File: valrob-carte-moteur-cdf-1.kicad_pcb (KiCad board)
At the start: 2 copper layers, 74 parts, among them J1 USB_C_Receptacle_USB2.0_14P, J2 Conn_01x02, J3 Conn_01x02, J4 Conn_01x04_Pin, J5 Conn_01x08, J6 Conn_01x02, J7 Conn_01x02, J8 Conn_01x08, SW1 SW_Push, SW2 SW_Push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

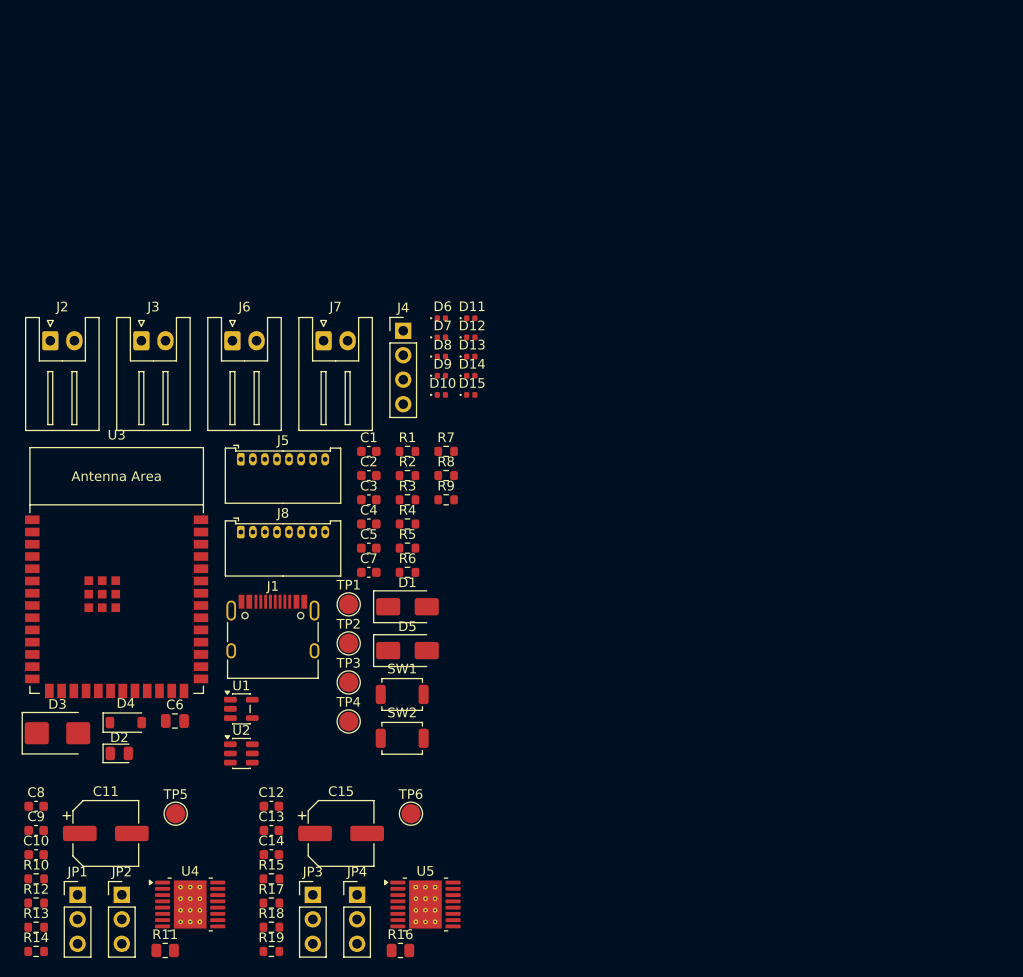
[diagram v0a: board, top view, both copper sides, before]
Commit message: pcb: initial rough placement
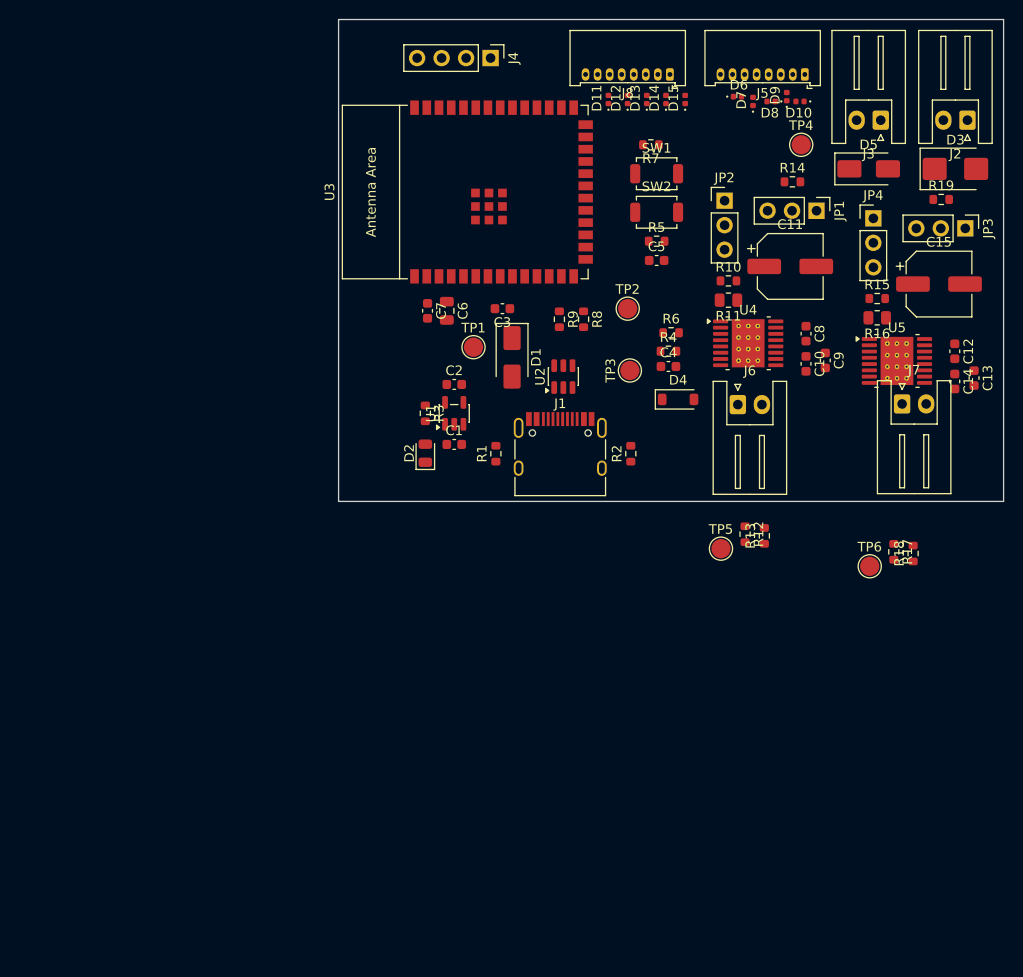
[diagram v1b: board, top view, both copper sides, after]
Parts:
- moved R14 112.0 mm to (124.1, 101.8)
- moved D3 110.0 mm to (141.0, 100.5)
- moved R19 104.5 mm to (139.5, 103.7)
- moved JP1 104.5 mm to (126.6, 104.8), turned to -90 degrees
- moved J2 97.9 mm to (142.2, 95.4), turned to 180 degrees
- moved JP3 96.8 mm to (142.0, 106.7), turned to -90 degrees
- moved JP2 95.4 mm to (117.0, 103.8)
- moved C9 95.3 mm to (127.5, 120.4), turned to -90 degrees
- moved R10 94.9 mm to (117.5, 112.1)
- moved C10 94.7 mm to (125.5, 120.7), turned to -90 degrees
- moved C8 93.7 mm to (125.5, 117.6), turned to -90 degrees
- moved C11 92.2 mm to (123.9, 110.6)
- moved R11 89.3 mm to (117.5, 114.1), turned to 180 degrees
- moved JP4 88.3 mm to (132.5, 105.6)
- moved R15 87.0 mm to (132.9, 113.9)
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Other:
- board outline added: 69 x 50 mm

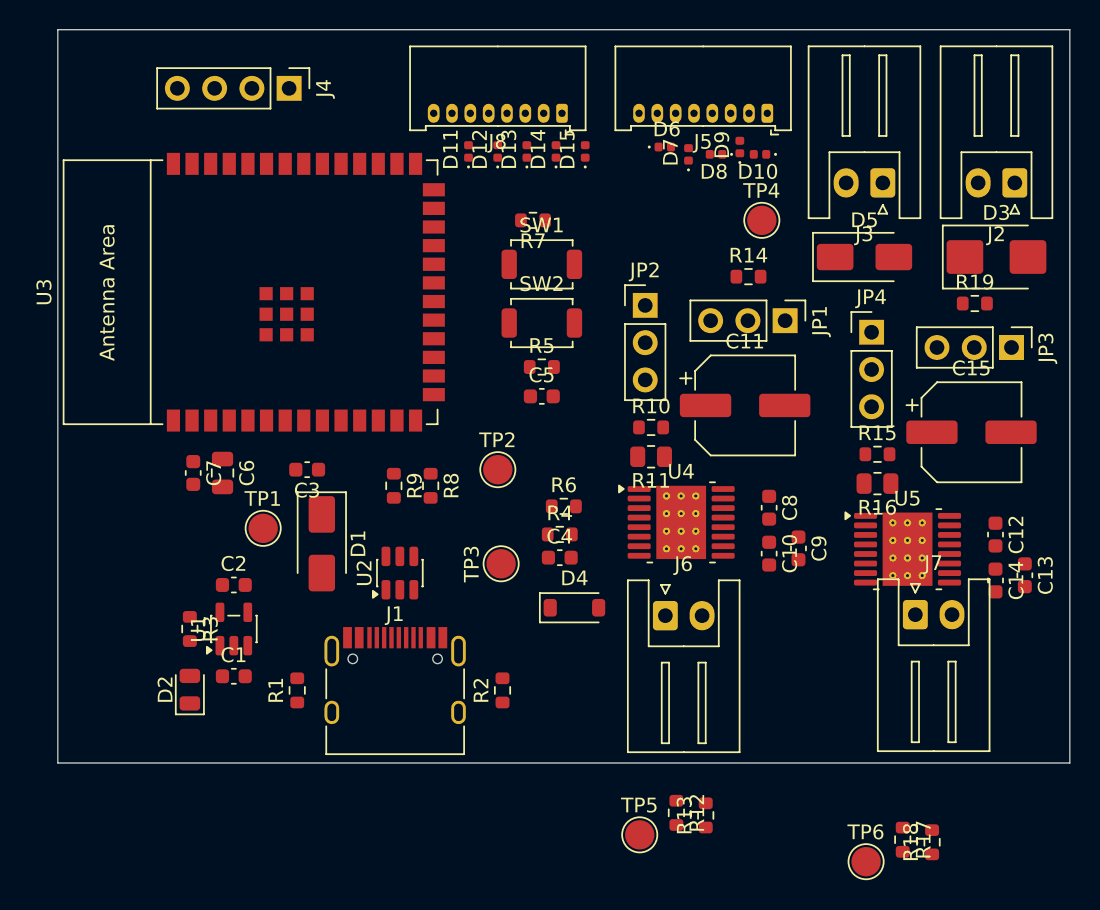
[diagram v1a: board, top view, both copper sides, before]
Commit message: pcb: add 4 M2 mounting holes
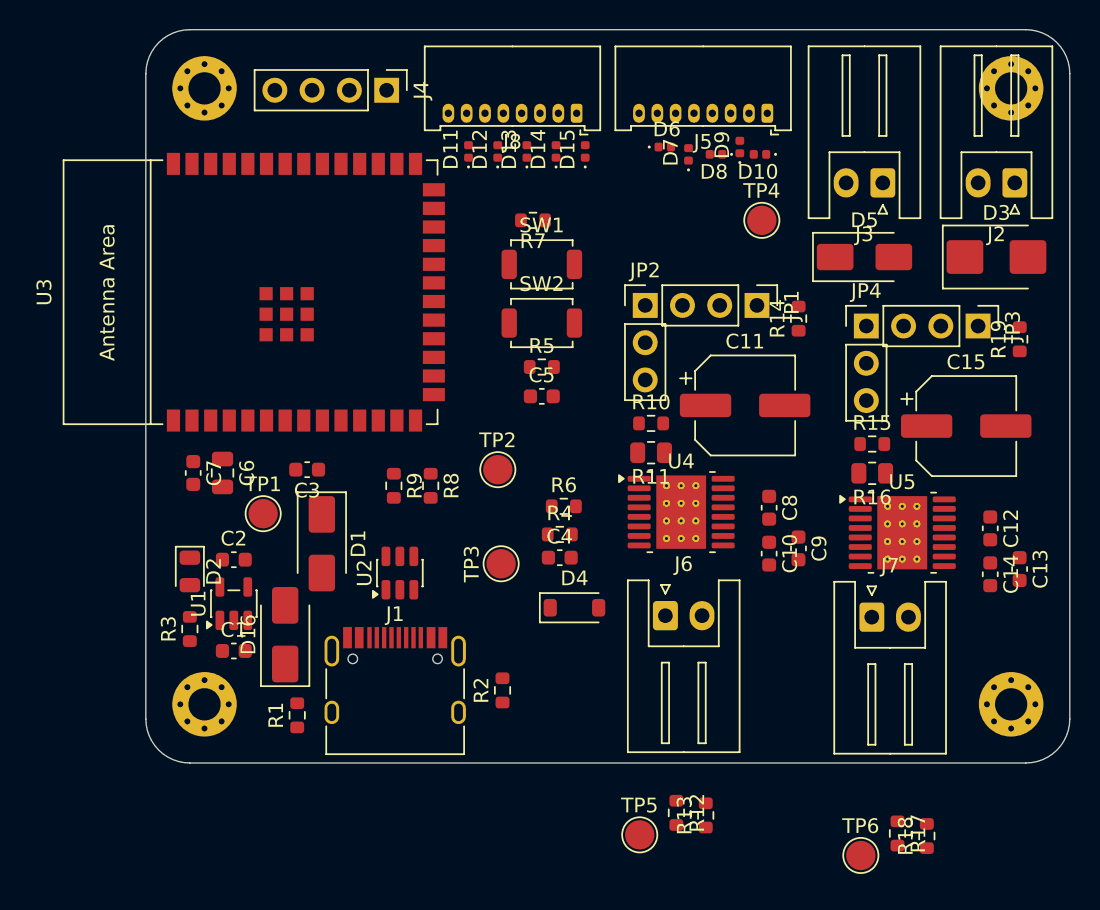
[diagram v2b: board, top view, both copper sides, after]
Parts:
- added D16: D_Schottky, Diode_SMD:D_SMA, F.Cu at (92.5, 126.2)
- added REF**: MountingHole_2.2mm_M2_Pad_Via, MountingHole:MountingHole_2.2mm_M2_Pad_Via, F.Cu at (142.0, 89.0)
- added REF**: MountingHole_2.2mm_M2_Pad_Via, MountingHole:MountingHole_2.2mm_M2_Pad_Via, F.Cu at (87.0, 131.0)
- added REF**: MountingHole_2.2mm_M2_Pad_Via, MountingHole:MountingHole_2.2mm_M2_Pad_Via, F.Cu at (142.0, 131.0)
- added REF**: MountingHole_2.2mm_M2_Pad_Via, MountingHole:MountingHole_2.2mm_M2_Pad_Via, F.Cu at (87.0, 89.0)
- moved D2 8.06 mm to (86.0, 121.9), turned to -90 degrees
- moved J4 6.65 mm to (99.4, 89.1)
- moved R14 4.46 mm to (127.5, 104.7), turned to 90 degrees
- moved R19 3.91 mm to (142.6, 106.1), turned to 90 degrees
- moved J7 2.97 mm to (132.5, 125.1)
- moved JP3 2.71 mm to (139.7, 105.2)
- moved JP1 2.18 mm to (124.7, 103.8)
- moved C1 1.73 mm to (89.0, 127.4)
- moved C2 1.72 mm to (89.0, 121.1)
- moved U1 1.72 mm to (89.0, 124.1)
- moved R1 1.70 mm to (93.3, 131.8)
- moved U5 1.18 mm to (134.6, 119.3)
- moved J8 1.00 mm to (112.4, 90.7)
- moved TP1 1.00 mm to (91.0, 118.0)
- moved R15 0.79 mm to (132.5, 113.2)
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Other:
- board size 69 x 50 mm -> 63 x 50 mm

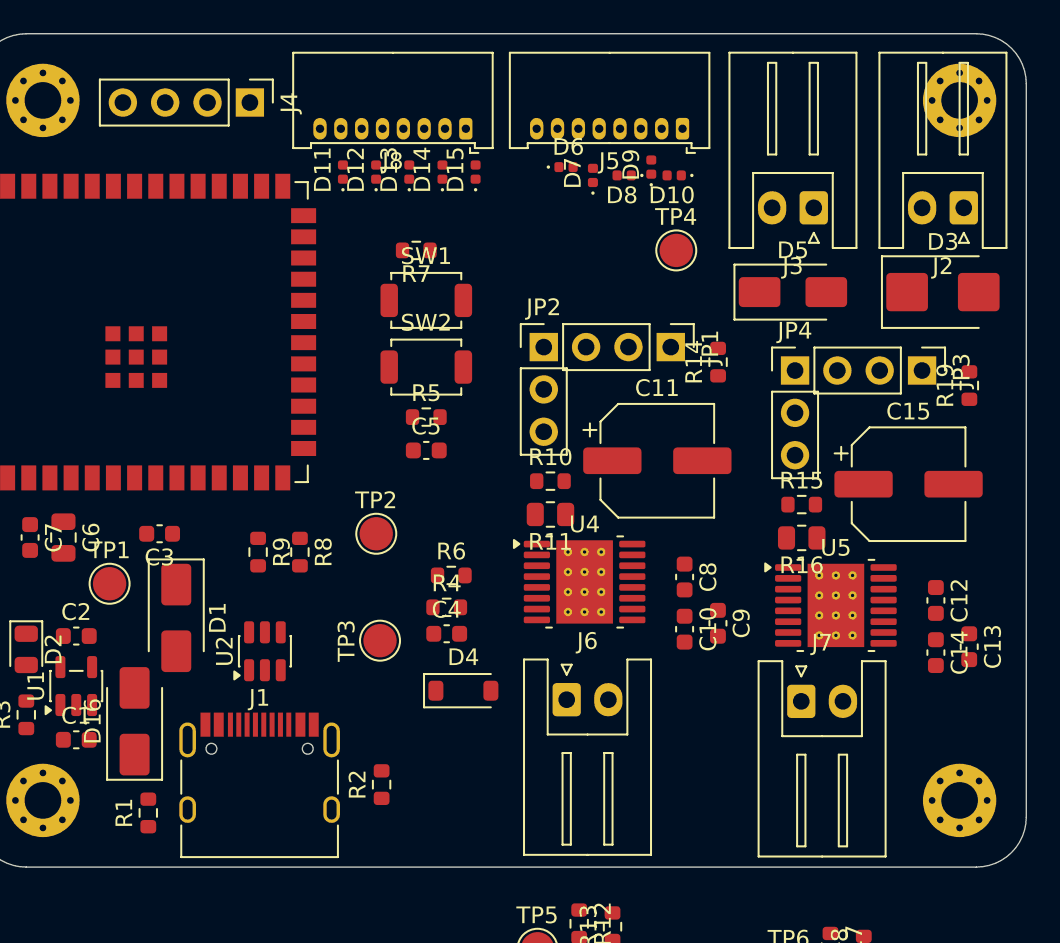
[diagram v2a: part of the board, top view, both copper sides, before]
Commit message: pcb: add fiducials and tooling holes
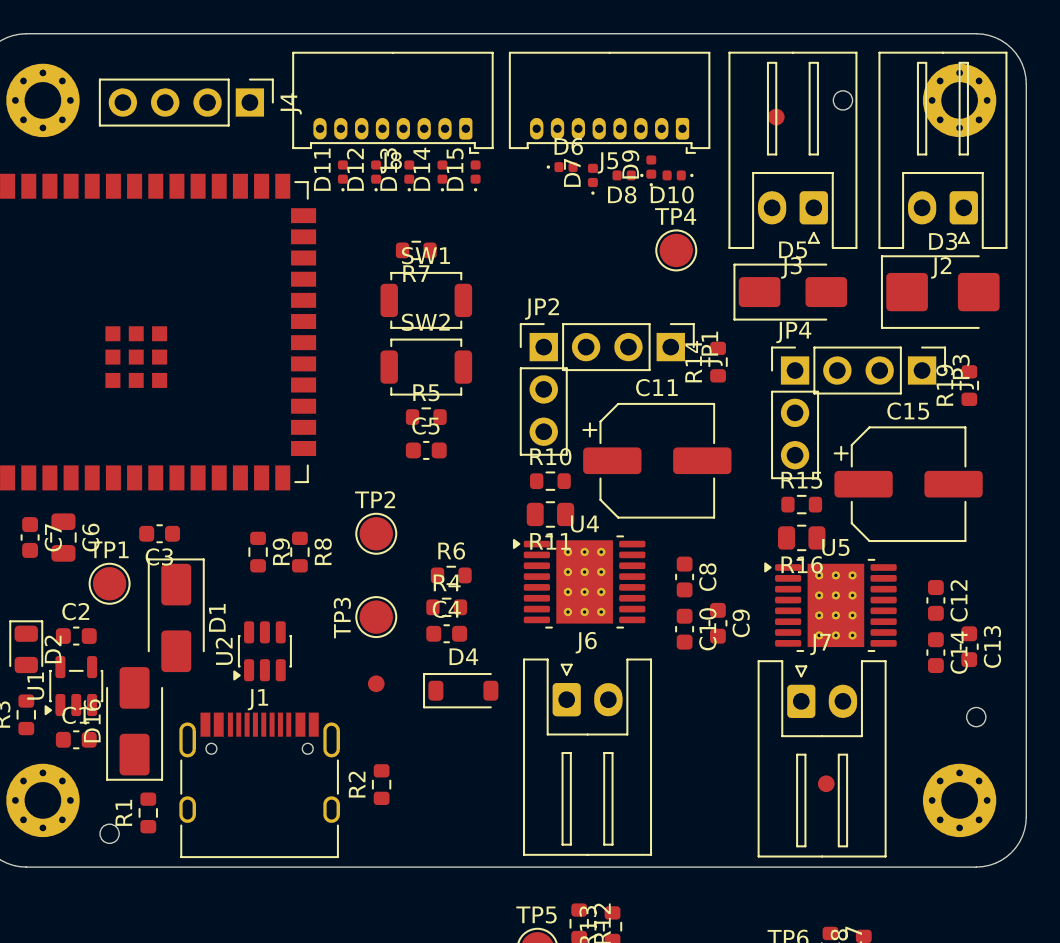
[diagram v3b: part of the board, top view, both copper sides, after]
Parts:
- added ?: , , F.Cu at (131.0, 90.0)
- added ?: , , F.Cu at (134.0, 130.0)
- added REF**: ToolingHole_1.152mm, MountingHole:ToolingHole_1.152mm, F.Cu at (91.0, 133.0)
- added REF**: ToolingHole_1.152mm, MountingHole:ToolingHole_1.152mm, F.Cu at (143.0, 126.0)
- added REF**: ToolingHole_1.152mm, MountingHole:ToolingHole_1.152mm, F.Cu at (135.0, 89.0)
- added REF**: Fiducial_1mm_Mask2mm, Fiducial:Fiducial_1mm_Mask2mm, F.Cu at (107.0, 124.0)
- moved TP3 1.43 mm to (107.0, 120.0)

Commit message: pcb: layout refinement
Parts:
- moved R18 61.7 mm to (97.5, 92.0), turned to 0 degrees
- moved R13 23.3 mm to (112.5, 117.0), turned to 180 degrees
- moved TP5 22.6 mm to (108.0, 119.0)
- moved R12 20.5 mm to (112.5, 119.0), turned to 180 degrees
- moved R17 20.4 mm to (129.5, 120.0), turned to 90 degrees
- moved TP2 19.7 mm to (117.0, 98.0)
- moved TP6 17.0 mm to (127.0, 125.0)
- moved C4 8.50 mm to (111.5, 129.5)
- moved R4 8.00 mm to (111.5, 127.4)
- moved R6 8.00 mm to (111.5, 125.5)
- moved D4 7.53 mm to (111.5, 131.9)
- moved C3 5.85 mm to (92.0, 120.5), turned to -90 degrees
- moved SW2 5.50 mm to (110.0, 110.5)
- moved TP3 5.15 mm to (111.5, 122.5)
- moved C5 4.50 mm to (110.0, 105.5), turned to 180 degrees
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
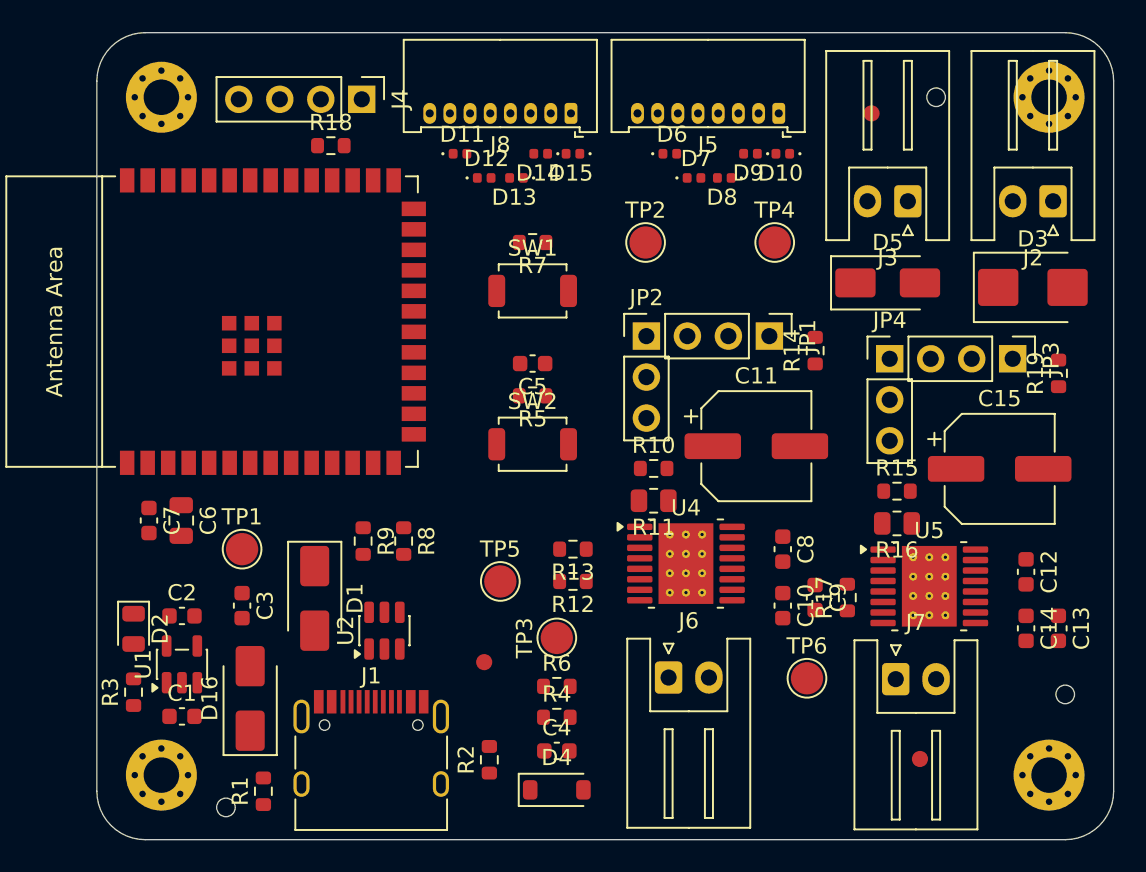
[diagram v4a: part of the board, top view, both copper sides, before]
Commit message: pcb: add gnd planes
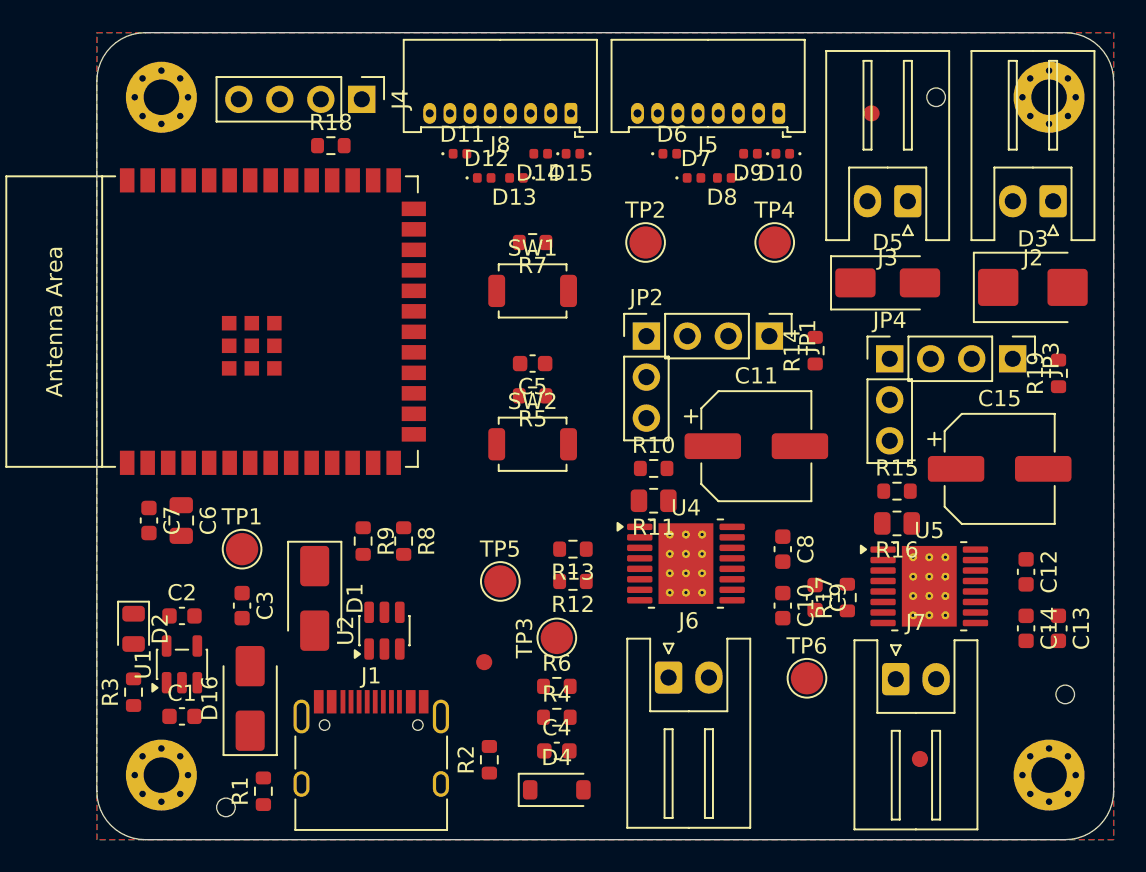
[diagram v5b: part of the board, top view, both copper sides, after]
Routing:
- added copper zone on B.Cu, net GND
- added copper zone on F.Cu, net GND
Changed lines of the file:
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@@
+	)
+	(zone
+		(net 1)
+		(net_name "GND")
+		(layers "F.Cu" "B.Cu")
+		(hatch edge 0.5)
+		(connect_pads
+			(clearance 0.2)
+		)
+		(min_thickness 0.15)
+		(filled_areas_thickness no)
+		(fill yes
+			(thermal_gap 0.35)
+			(thermal_bridge_width 0.35)
+		)
+		(polygon
+			(pts
+				(xy 83 135) (xy 83 85) (xy 146 85) (xy 146 135)
+			)
+		)
 	)
 	(zone
